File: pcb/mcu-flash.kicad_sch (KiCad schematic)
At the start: 26 parts, among them J1 0015910100, SW1 SW_Push, U1 W25Q128JVS, U2 RP2040, Y1 ABM8AIG-12.000MHZ-12-2Z-T3

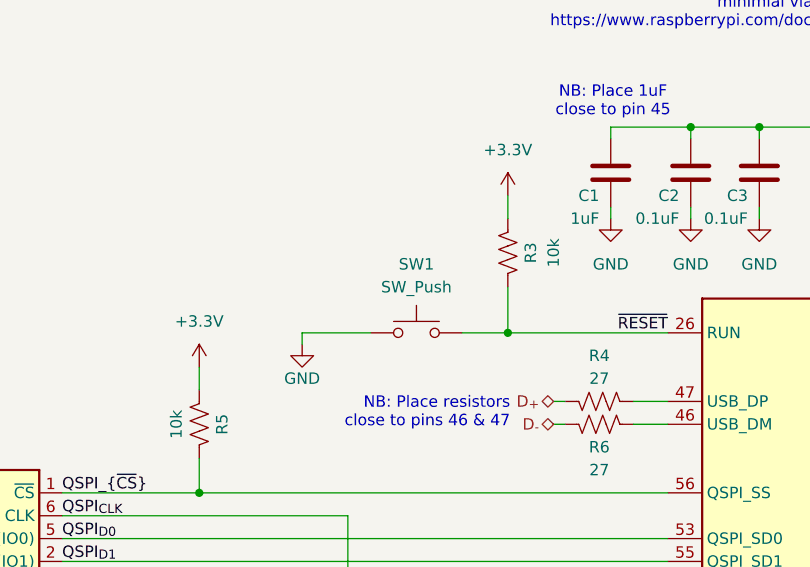
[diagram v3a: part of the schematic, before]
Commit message: Revision D of controller PCB
- Small changes during PCB review
- This commit will be fabricated
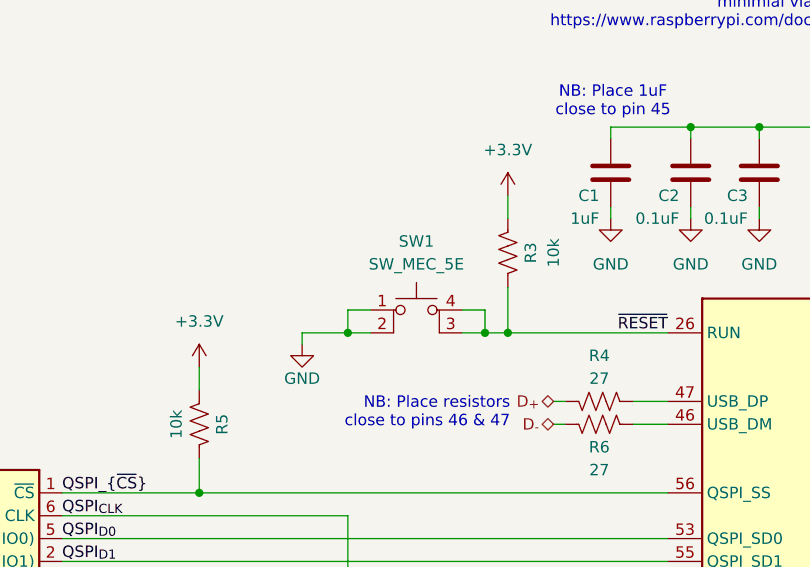
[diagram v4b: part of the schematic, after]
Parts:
- removed SW1: SW_Push, Button_Switch_SMD:SW_Push_1P1T_NO_CK_KMR2, symbol Switch:SW_Push
- added SW1: SW_MEC_5E, oe:PANASONIC_EVQP7-JA-01P, symbol Switch:SW_MEC_5E
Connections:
- net GND: now also SW1.1, SW1.2
- net ~{RESET}: now also SW1.3 (K), SW1.4 (A)
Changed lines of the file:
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@@
 	)
 	(junction
+		(at 81.28 63.5)
+		(diameter 0)
+		(color 0 0 0 0)
+	)
+	(junction
 		(at 186.69 40.64)
 		(diameter 0)
@@
 		(color 0 0 0 0)
 	)
+	(junction
+		(at 96.52 63.5)
+		(diameter 0)
+		(color 0 0 0 0)
+	)
 	(no_connect
 		(at 167.64 124.46)
@@
 	(wire
 		(pts
+			(xy 93.98 60.96) (xy 96.52 60.96)
+		)
+		(stroke
+			(width 0)
+			(type default)
+		)
+	)
+	(wire
+		(pts
 			(xy 78.74 109.22) (xy 78.74 110.49)
 		)
@@
 	(wire
 		(pts
+			(xy 96.52 63.5) (xy 99.06 63.5)
+		)
+		(stroke
+			(width 0)
+			(type default)
+		)
+	)
+	(wire
+		(pts
 			(xy 144.78 40.64) (xy 147.32 40.64)
 		)
@@
 	(wire
 		(pts
+			(xy 96.52 60.96) (xy 96.52 63.5)
+		)
+		(stroke
+			(width 0)
+			(type default)
+		)
+	)
+	(wire
+		(pts
 			(xy 168.91 106.68) (xy 167.64 106.68)
 		)
@@
 	(wire
 		(pts
-			(xy 93.98 63.5) (xy 99.06 63.5)
+			(xy 83.82 60.96) (xy 81.28 60.96)
+		)
+		(stroke
+			(width 0)
+			(type default)
+		)
+	)
+	(wire
+		(pts
+			(xy 93.98 63.5) (xy 96.52 63.5)
 		)
 		(stroke
@@
 	(wire
 		(pts
-			(xy 76.2 63.5) (xy 83.82 63.5)
+			(xy 76.2 63.5) (xy 81.28 63.5)
 		)
 		(stroke
@@
 	(wire
 		(pts
+			(xy 81.28 60.96) (xy 81.28 63.5)
+		)
+		(stroke
+			(width 0)
+			(type default)
+		)
+	)
+	(wire
+		(pts
 			(xy 149.86 40.64) (xy 149.86 55.88)
 		)
@@
 	(wire
 		(pts
+			(xy 81.28 63.5) (xy 83.82 63.5)
+		)
+		(stroke
+			(width 0)
+			(type default)
+		)
+	)
+	(wire
+		(pts
 			(xy 201.93 49.53) (xy 201.93 50.8)
 		)
@@
 	)
 	(symbol
+		(lib_id "Switch:SW_MEC_5E")
+		(at 88.9 63.5 0)
+		(unit 1)
+		(exclude_from_sim no)
+		(in_bom yes)
+		(on_board yes)
+		(dnp no)
+		(fields_autoplaced yes)
+		(property "Reference" "SW1"
+			(at 88.9 53.34 0)
+			(effects
+				(font
+					(size 1.27 1.27)
+				)
+			)
+		)
+		(property "Value" "SW_MEC_5E"
+			(at 88.9 55.88 0)
+			(effects
+				(font
+					(size 1.27 1.27)
+				)
+			)
+		)
+		(property "Footprint" "oe:PANASONIC_EVQP7-JA-01P"
+			(at 88.9 55.88 0)
+			(effects
+				(font
+					(size 1.27 1.27)
+				)
+				(hide yes)
+			)
+		)
+		(property "Datasheet" "http://www.apem.com/int/index.php?controller=attachment&id_attachment=1371"
+			(at 88.9 55.88 0)
+			(effects
+				(font
+					(size 1.27 1.27)
+				)
+				(hide yes)
+			)
+		)
+		(property "Description" "MEC 5E single pole normally-open tactile switch"
+			(at 88.9 63.5 0)
+			(effects
+				(font
+					(size 1.27 1.27)
+				)
+				(hide yes)
+			)
+		)
+		(pin "2"
+		)
+		(pin "3"
+		)
+		(pin "4"
+		)
+		(pin "1"
+		)
+		(instances
+			(project ""
+				(path "/f8e1d654-dc44-4fb2-953c-f5982945ff40/f332ab09-c494-4f8f-98bf-7facb28de9af"
+					(reference "SW1")
+					(unit 1)
+				)
+			)
+		)
+	)
+	(symbol
 		(lib_id "Device:R_US")
 		(at 109.22 73.66 270)
@@
 					(unit 1)
 				)
-			)
-		)
-	)
-	(symbol
-		(lib_id "Switch:SW_Push")
-		(at 88.9 63.5 0)
-		(unit 1)
-		(exclude_from_sim no)
-		(in_bom yes)
-		(on_board yes)
-		(dnp no)
-		(fields_autoplaced yes)
-		(property "Reference" "SW1"
-			(at 88.9 55.88 0)
-			(effects
-				(font
-					(size 1.27 1.27)
-				)
-			)
-		)
-		(property "Value" "SW_Push"
-			(at 88.9 58.42 0)
-			(effects
-				(font
-					(size 1.27 1.27)
-				)
-			)
-		)
-		(property "Footprint" "Button_Switch_SMD:SW_Push_1P1T_NO_CK_KMR2"
-			(at 88.9 58.42 0)
-			(effects
-				(font
-					(size 1.27 1.27)
-				)
-				(hide yes)
-			)
-		)
-		(property "Datasheet" "https://www.ckswitches.com/media/1479/kmr2.pdf"
-			(at 88.9 58.42 0)
-			(effects
-				(font
-					(size 1.27 1.27)
-				)
-				(hide yes)
-			)
-		)
-		(property "Description" "Push button switch, generic, two pins"
-			(at 88.9 63.5 0)
-			(effects
-				(font
-					(size 1.27 1.27)
-				)
-				(hide yes)
-			)
-		)
-		(pin "1"
-		)
-		(pin "2"
-		)
-		(instances
-			(project "oe-commutator-controller"
-				(path "/f8e1d654-dc44-4fb2-953c-f5982945ff40/f332ab09-c494-4f8f-98bf-7facb28de9af"
-					(reference "SW1")
-					(unit 1)
-				)
